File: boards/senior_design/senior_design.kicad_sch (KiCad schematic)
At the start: 20 parts, among them J1 Conn_01x04, U11 UA741CP, U3 AD620, U4 AD630ARZ, U7 UA741CP

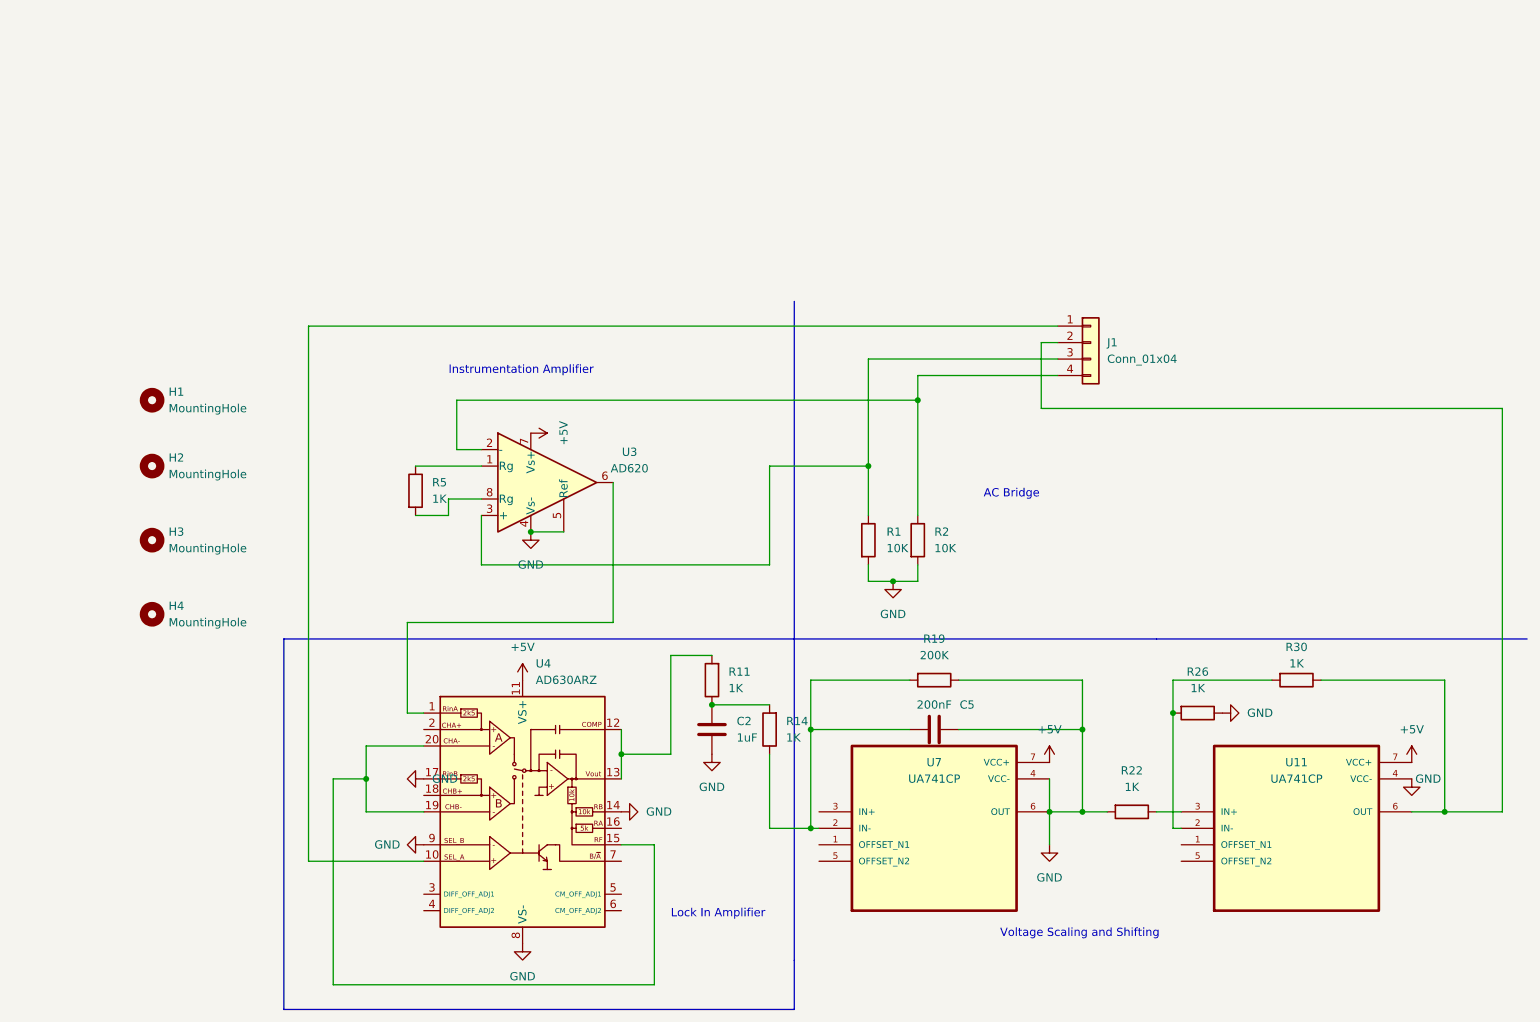
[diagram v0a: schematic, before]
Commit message: Revert "Merge branch 'main' of github.com:keeratS/445team27 into main"
This reverts commit 777689c8a8ad57f7277eda5b46fe19858a00a95d, reversing
changes made to 7e022650be9491f24625faac10ecfe32b749daf8.
undoing mistaken merge
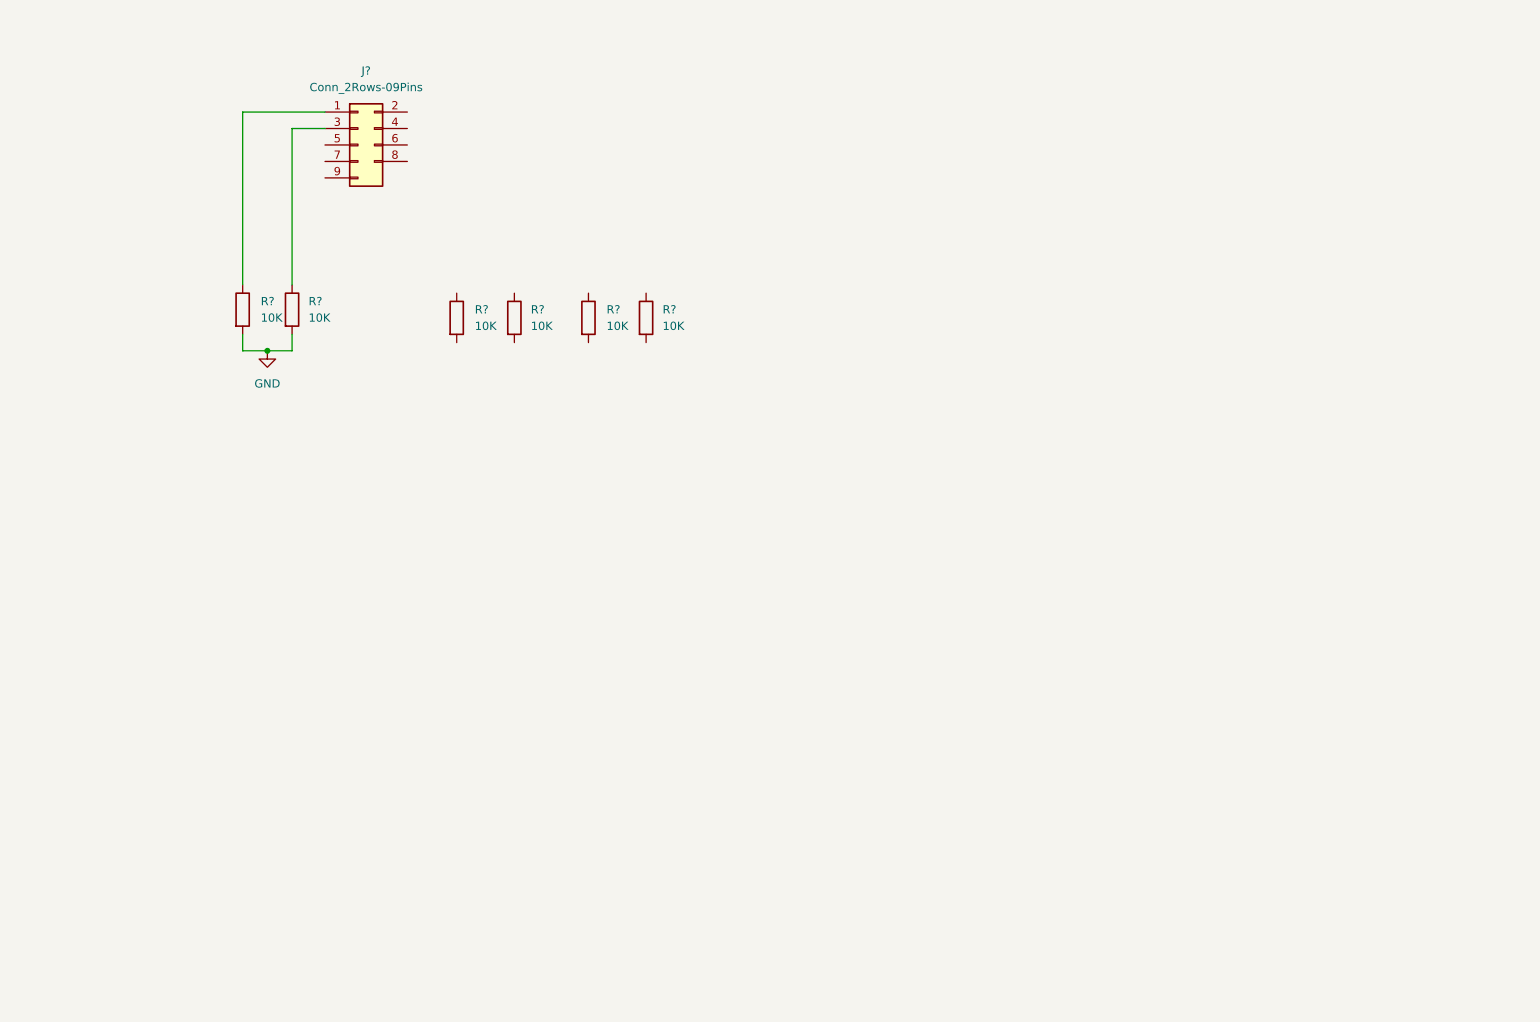
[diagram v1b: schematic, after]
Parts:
- removed C2: 1uF, Capacitor_SMD:C_0805_2012Metric_Pad1.18x1.45mm_HandSolder, symbol Device:C
- removed C5: 200nF, Capacitor_SMD:C_0805_2012Metric_Pad1.18x1.45mm_HandSolder, symbol Device:C
- removed H1, H2, H3, H4: MountingHole, MountingHole:MountingHole_3.2mm_M3, symbol Mechanical:MountingHole
- removed J1: Conn_01x04, Connector_Molex:Molex_KK-254_AE-6410-04A_1x04_P2.54mm_Vertical, symbol Connector_Generic:Conn_01x04
- removed R11, R14, R22, R26, R30, R5: 1K, Resistor_SMD:R_0805_2012Metric_Pad1.20x1.40mm_HandSolder, symbol Device:R
- removed R19: 200K, Resistor_SMD:R_0805_2012Metric_Pad1.20x1.40mm_HandSolder, symbol Device:R
- removed U11, U7: UA741CP, uA741:DIP794W45P254L959H508Q8, symbol uA741:UA741CP
- removed U3: AD620, AD620:DIL08, symbol Amplifier_Instrumentation:AD620
- removed U4: AD630ARZ, Package_SO:SOIC-20W_7.5x12.8mm_P1.27mm, symbol Analog:AD630ARZ
- added J?: Conn_2Rows-09Pins, symbol Connector_Generic:Conn_2Rows-09Pins
- added R? (x4): 10K, symbol Device:R
- R?: renamed from R2; footprint Resistor_SMD:R_0805_2012Metric_Pad1.20x1.40mm_HandSolder -> (none)
- R?: renamed from R1; footprint Resistor_SMD:R_0805_2012Metric_Pad1.20x1.40mm_HandSolder -> (none)
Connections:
- net at R?.1: now also J?.1 (Pin_1)
- net at R?.1: now also J?.3 (Pin_3)
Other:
- note removed: "AC Bridge"
- note removed: "Instrumentation Amplifier"
- note removed: "Lock In Amplifier"
- note removed: "Voltage Scaling and Shifting"
- moved on the sheet: R?

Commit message: added balanced demodulator to schematic
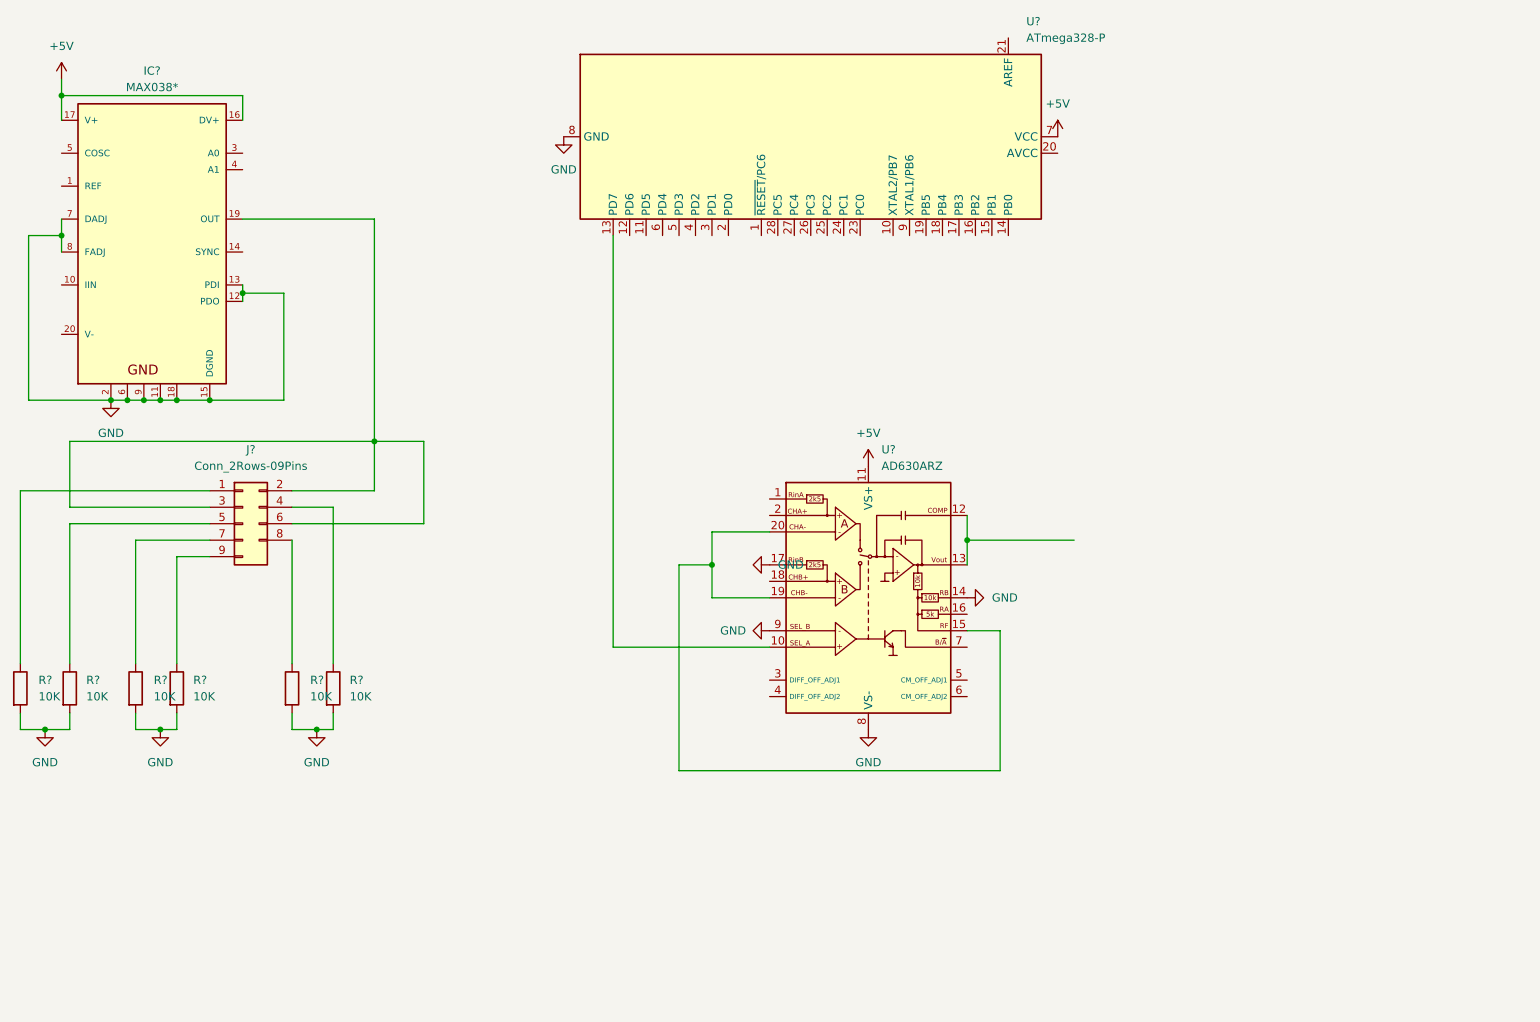
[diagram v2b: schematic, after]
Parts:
- removed R? (x2): 10K, symbol Device:R
- added IC?: MAX038*, symbol MAX038_:MAX038*
- added R? (x2): 10K, symbol Device:R
- added U?: ATmega328-P, Package_DIP:DIP-28_W7.62mm, symbol MCU_Microchip_ATmega:ATmega328-P
- added U?: AD630ARZ, Package_SO:SOIC-20W_7.5x12.8mm_P1.27mm, symbol Analog:AD630ARZ
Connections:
- net GND: now also R?.2, R?.2, IC?.11, IC?.12 (PDO), IC?.13 (PDI), IC?.15 (DGND), IC?.18, IC?.2, IC?.6, IC?.7 (DADJ), IC?.8 (FADJ), IC?.9, R?.2, R?.2, U?.14 (RB), U?.17 (RinB), U?.22 (GND), U?.8 (GND), U?.8 (VS-), U?.9 (SEL_B)
- net at R?.1: now also J?.7 (Pin_7)
- net at R?.1: now also J?.9 (Pin_9)
- net at J?.2 (Pin_2): now also J?.3 (Pin_3), J?.6 (Pin_6), IC?.19 (OUT)
- net at R?.1: now also J?.5 (Pin_5); no longer J?.3 (Pin_3)
- net at J?.4 (Pin_4): now also R?.1
- net at J?.8 (Pin_8): now also R?.1
- new net: U?.10 (SEL_A), U?.13 (PD7)
- new net: U?.12 (COMP), U?.13 (Vout)
- new net: U?.15 (RF), U?.19 (CHB-), U?.20 (CHA-)
- new net +5V: IC?.16 (DV+), IC?.17 (V+), U?.11 (VS+), U?.7 (VCC)
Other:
- moved on the sheet: J?, R?
